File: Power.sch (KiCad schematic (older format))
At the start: 0 parts

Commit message: Power protection and filtering circuit moved to Power.sch, was accidentally on PowerAdjustmentMonitor.sch
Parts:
- added C? (x2): C, symbol C
- added F? (x4): FUSE, symbol FUSE
- added L? (x2): INDUCTOR, symbol INDUCTOR
- added P?: CONN_12X2, symbol CONN_12X2
- added R?: R, symbol R
- added SW?: SWITCH_INV, symbol SWITCH_INV
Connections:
- net labels added: +12P, +12V, +3.3V, +5V, -12P, -12V, GND
- wire segments 0 -> 39

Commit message: Current/fan driver circuit reworked
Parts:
- removed F? (x4): FUSE, symbol FUSE
- added TH? (x4): THERMISTOR, symbol THERMISTOR
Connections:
- net labels added: +12C
- wire segments 39 -> 40
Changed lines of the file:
@@
 $Descr A4 11693 8268
 encoding utf-8
-Sheet 5 9
+Sheet 4 9
 Title ""
 Date ""
@@
 	900  1900 900  2100
 $Comp
-L FUSE F?
-U 1 1 52F29C98
-P 3250 1800
-F 0 "F?" H 3350 1850 40  0000 C CNN
-F 1 "FUSE" H 3150 1750 40  0000 C CNN
-F 2 "" H 3250 1800 60  0000 C CNN
-F 3 "" H 3250 1800 60  0000 C CNN
-	1    3250 1800
-	1    0    0    -1
-$EndComp
-$Comp
-L FUSE F?
-U 1 1 52F29C9E
-P 3750 2000
-F 0 "F?" H 3850 2050 40  0000 C CNN
-F 1 "FUSE" H 3650 1950 40  0000 C CNN
-F 2 "" H 3750 2000 60  0000 C CNN
-F 3 "" H 3750 2000 60  0000 C CNN
-	1    3750 2000
-	1    0    0    -1
-$EndComp
-$Comp
-L FUSE F?
-U 1 1 52F29CA4
-P 4250 2200
-F 0 "F?" H 4350 2250 40  0000 C CNN
-F 1 "FUSE" H 4150 2150 40  0000 C CNN
-F 2 "" H 4250 2200 60  0000 C CNN
-F 3 "" H 4250 2200 60  0000 C CNN
-	1    4250 2200
-	1    0    0    -1
-$EndComp
-$Comp
-L FUSE F?
-U 1 1 52F29CAA
-P 4750 2400
-F 0 "F?" H 4850 2450 40  0000 C CNN
-F 1 "FUSE" H 4650 2350 40  0000 C CNN
-F 2 "" H 4750 2400 60  0000 C CNN
-F 3 "" H 4750 2400 60  0000 C CNN
-	1    4750 2400
-	1    0    0    -1
-$EndComp
-$Comp
 L SWITCH_INV SW?
 U 1 1 52F29CB0
@@
 	-1   0    0    1
 $EndComp
+Connection ~ 2800 2200
+Wire Wire Line
+	2800 2200 2800 1550
+$Comp
+L +12C #PWR?
+U 1 1 52FBE7EF
+P 2800 1550
+F 0 "#PWR?" H 2800 1520 30  0001 C CNN
+F 1 "+12C" H 2800 1660 40  0000 C CNN
+F 2 "" H 2800 1550 60  0000 C CNN
+F 3 "" H 2800 1550 60  0000 C CNN
+	1    2800 1550
+	1    0    0    -1
+$EndComp
+$Comp
+L THERMISTOR TH?
+U 1 1 52FBEC4C
+P 3250 1800
+F 0 "TH?" V 3350 1850 50  0000 C CNN
+F 1 "THERMISTOR" V 3150 1800 50  0000 C CNN
+F 2 "" H 3250 1800 60  0000 C CNN
+F 3 "" H 3250 1800 60  0000 C CNN
+	1    3250 1800
+	0    -1   -1   0
+$EndComp
+$Comp
+L THERMISTOR TH?
+U 1 1 52FBEC68
+P 3750 2000
+F 0 "TH?" V 3850 2050 50  0000 C CNN
+F 1 "THERMISTOR" V 3650 2000 50  0000 C CNN
+F 2 "" H 3750 2000 60  0000 C CNN
+F 3 "" H 3750 2000 60  0000 C CNN
+	1    3750 2000
+	0    -1   -1   0
+$EndComp
+$Comp
+L THERMISTOR TH?
+U 1 1 52FBEC73
+P 4250 2200
+F 0 "TH?" V 4350 2250 50  0000 C CNN
+F 1 "THERMISTOR" V 4150 2200 50  0000 C CNN
+F 2 "" H 4250 2200 60  0000 C CNN
+F 3 "" H 4250 2200 60  0000 C CNN
+	1    4250 2200
+	0    -1   -1   0
+$EndComp
+$Comp
+L THERMISTOR TH?
+U 1 1 52FBEC7E
+P 4750 2400
+F 0 "TH?" V 4850 2450 50  0000 C CNN
+F 1 "THERMISTOR" V 4650 2400 50  0000 C CNN
+F 2 "" H 4750 2400 60  0000 C CNN
+F 3 "" H 4750 2400 60  0000 C CNN
+	1    4750 2400
+	0    -1   -1   0
+$EndComp
 $EndSCHEMATC

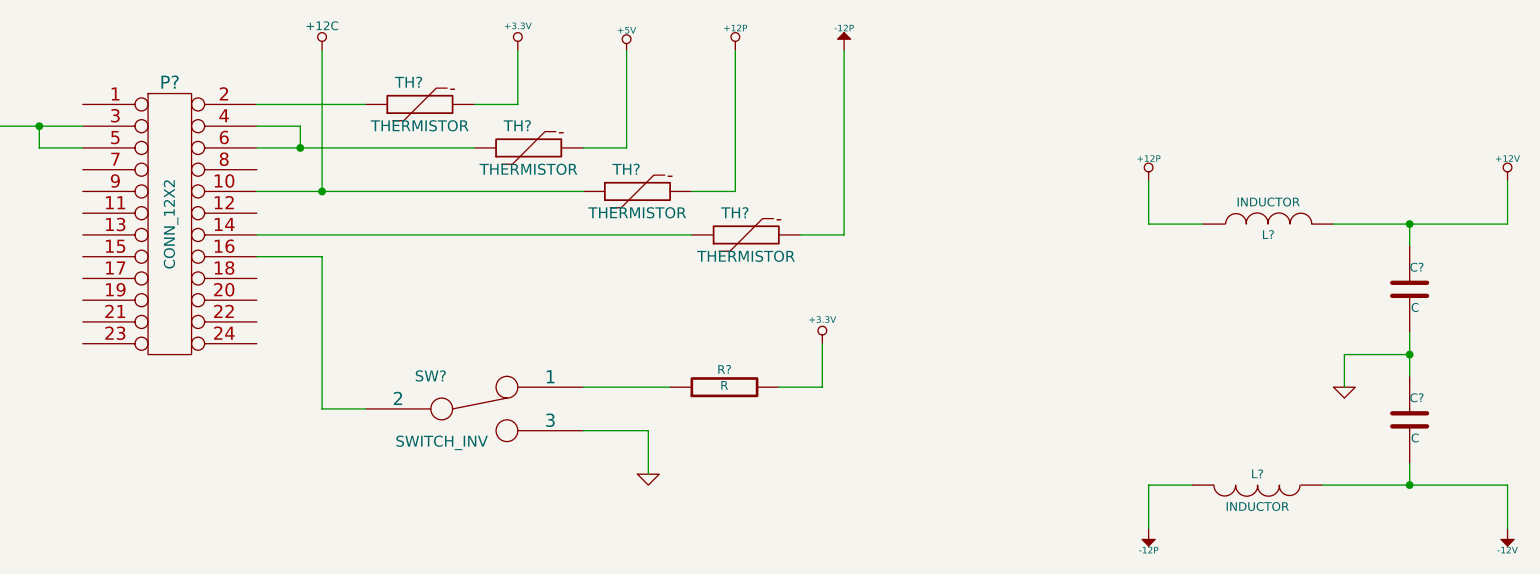
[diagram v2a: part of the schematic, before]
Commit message: Added footprints for the relay module, preliminarily annotated schematic, relay components placed on PCB
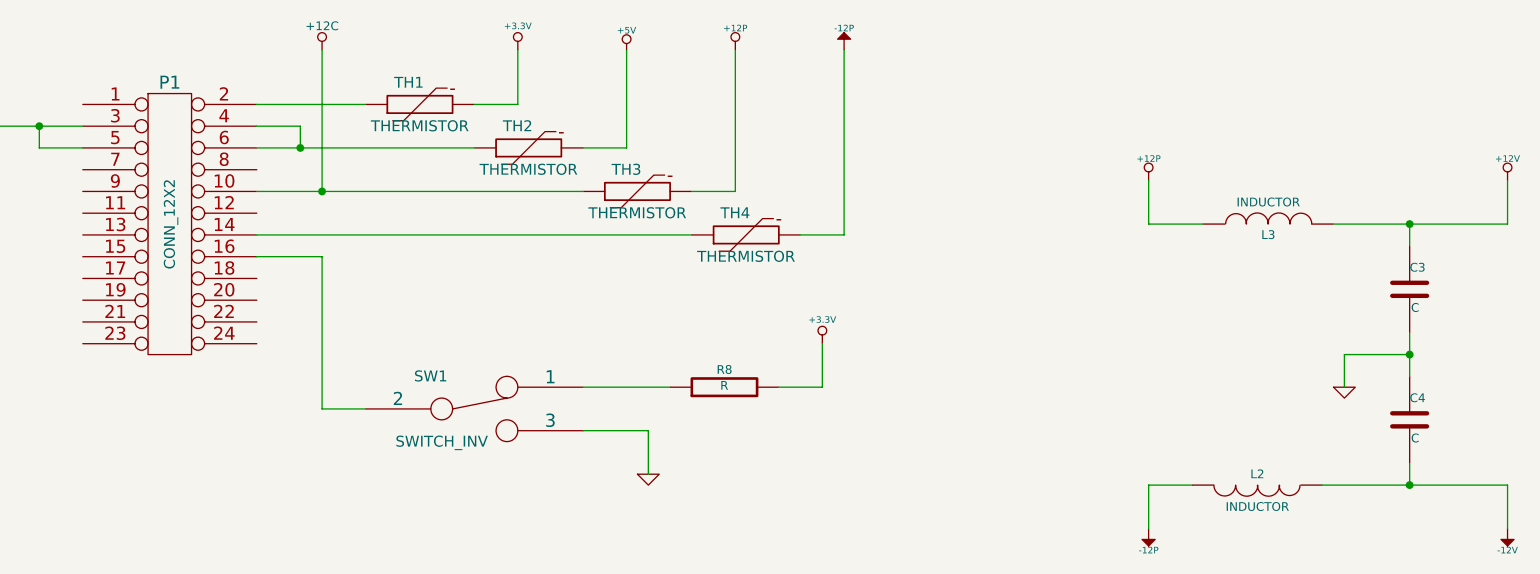
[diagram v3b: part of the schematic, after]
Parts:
- gave numbers to parts that had none: 11
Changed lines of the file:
@@
 $EndDescr
 $Comp
-L CONN_12X2 P?
+L CONN_12X2 P1
 U 1 1 52F29C7F
 P 2100 2350
-F 0 "P?" H 2100 3000 60  0000 C CNN
+F 0 "P1" H 2100 3000 60  0000 C CNN
 F 1 "CONN_12X2" V 2100 2350 50  0000 C CNN
 F 2 "" H 2100 2350 60  0000 C CNN
@@
 $EndComp
 $Comp
-L GND #PWR?
+L GND #PWR7
 U 1 1 52F29C85
 P 900 2100
-F 0 "#PWR?" H 900 2100 30  0001 C CNN
+F 0 "#PWR7" H 900 2100 30  0001 C CNN
 F 1 "GND" H 900 2030 30  0001 C CNN
 F 2 "" H 900 2100 60  0000 C CNN
@@
 $EndComp
 $Comp
-L +3.3V #PWR?
+L +3.3V #PWR9
 U 1 1 52F29C8B
 P 3700 1550
-F 0 "#PWR?" H 3700 1510 30  0001 C CNN
+F 0 "#PWR9" H 3700 1510 30  0001 C CNN
 F 1 "+3.3V" H 3700 1660 30  0000 C CNN
 F 2 "" H 3700 1550 60  0000 C CNN
@@
 $EndComp
 $Comp
-L +5V #PWR?
+L +5V #PWR10
 U 1 1 52F29C91
 P 4200 1550
-F 0 "#PWR?" H 4200 1640 20  0001 C CNN
+F 0 "#PWR10" H 4200 1640 20  0001 C CNN
 F 1 "+5V" H 4200 1640 30  0000 C CNN
 F 2 "" H 4200 1550 60  0000 C CNN
@@
 	900  1900 900  2100
 $Comp
-L SWITCH_INV SW?
+L SWITCH_INV SW1
 U 1 1 52F29CB0
 P 3500 3200
-F 0 "SW?" H 3300 3350 50  0000 C CNN
+F 0 "SW1" H 3300 3350 50  0000 C CNN
 F 1 "SWITCH_INV" H 3350 3050 50  0000 C CNN
 F 2 "" H 3500 3200 60  0000 C CNN
@@
 	4700 2200 4700 1550
 $Comp
-L +12P #PWR?
+L +12P #PWR12
 U 1 1 52F29CC3
 P 4700 1550
-F 0 "#PWR?" H 4700 1520 30  0001 C CNN
+F 0 "#PWR12" H 4700 1520 30  0001 C CNN
 F 1 "+12P" H 4700 1650 30  0000 C CNN
 F 2 "" H 4700 1550 60  0000 C CNN
@@
 	5200 2400 5200 1550
 $Comp
-L -12P #PWR?
+L -12P #PWR14
 U 1 1 52F29CCB
 P 5200 1550
-F 0 "#PWR?" H 5200 1680 20  0001 C CNN
+F 0 "#PWR14" H 5200 1680 20  0001 C CNN
 F 1 "-12P" H 5200 1650 30  0000 C CNN
 F 2 "" H 5200 1550 60  0000 C CNN
@@
 	4300 3300 4300 3500
 $Comp
-L GND #PWR?
+L GND #PWR11
 U 1 1 52F29CDA
 P 4300 3500
-F 0 "#PWR?" H 4300 3500 30  0001 C CNN
+F 0 "#PWR11" H 4300 3500 30  0001 C CNN
 F 1 "GND" H 4300 3430 30  0001 C CNN
 F 2 "" H 4300 3500 60  0000 C CNN
@@
 $EndComp
 $Comp
-L R R?
+L R R8
 U 1 1 52F29CE0
 P 4650 3100
-F 0 "R?" V 4730 3100 40  0000 C CNN
+F 0 "R8" V 4730 3100 40  0000 C CNN
 F 1 "R" V 4657 3101 40  0000 C CNN
 F 2 "" V 4580 3100 30  0000 C CNN
@@
 	5100 3100 5100 2900
 $Comp
-L +3.3V #PWR?
+L +3.3V #PWR13
 U 1 1 52F29CE9
 P 5100 2900
-F 0 "#PWR?" H 5100 2860 30  0001 C CNN
+F 0 "#PWR13" H 5100 2860 30  0001 C CNN
 F 1 "+3.3V" H 5100 3010 30  0000 C CNN
 F 2 "" H 5100 2900 60  0000 C CNN
@@
 $EndComp
 $Comp
-L +12P #PWR?
+L +12P #PWR15
 U 1 1 52F29CEF
 P 6600 2150
-F 0 "#PWR?" H 6600 2120 30  0001 C CNN
+F 0 "#PWR15" H 6600 2120 30  0001 C CNN
 F 1 "+12P" H 6600 2250 30  0000 C CNN
 F 2 "" H 6600 2150 60  0000 C CNN
@@
 $EndComp
 $Comp
-L -12P #PWR?
+L -12P #PWR16
 U 1 1 52F29CF5
 P 6600 3750
-F 0 "#PWR?" H 6600 3880 20  0001 C CNN
+F 0 "#PWR16" H 6600 3880 20  0001 C CNN
 F 1 "-12P" H 6600 3850 30  0000 C CNN
 F 2 "" H 6600 3750 60  0000 C CNN
@@
 $EndComp
 $Comp
-L GND #PWR?
+L GND #PWR17
 U 1 1 52F29CFB
 P 7500 3100
-F 0 "#PWR?" H 7500 3100 30  0001 C CNN
+F 0 "#PWR17" H 7500 3100 30  0001 C CNN
 F 1 "GND" H 7500 3030 30  0001 C CNN
 F 2 "" H 7500 3100 60  0000 C CNN
@@
 $EndComp
 $Comp
-L INDUCTOR L?
+L INDUCTOR L3
 U 1 1 52F29D01
 P 7150 2350
-F 0 "L?" V 7100 2350 40  0000 C CNN
+F 0 "L3" V 7100 2350 40  0000 C CNN
 F 1 "INDUCTOR" V 7250 2350 40  0000 C CNN
 F 2 "" H 7150 2350 60  0000 C CNN
@@
 $EndComp
 $Comp
-L INDUCTOR L?
+L INDUCTOR L2
 U 1 1 52F29D07
 P 7100 3550
-F 0 "L?" V 7050 3550 40  0000 C CNN
+F 0 "L2" V 7050 3550 40  0000 C CNN
 F 1 "INDUCTOR" V 7200 3550 40  0000 C CNN
 F 2 "" H 7100 3550 60  0000 C CNN
@@
 $EndComp
 $Comp
-L C C?
+L C C4
 U 1 1 52F29D0D
 P 7800 3250
-F 0 "C?" H 7800 3350 40  0000 L CNN
+F 0 "C4" H 7800 3350 40  0000 L CNN
 F 1 "C" H 7806 3165 40  0000 L CNN
 F 2 "" H 7838 3100 30  0000 C CNN
@@
 $EndComp
 $Comp
-L C C?
+L C C3
 U 1 1 52F29D13
 P 7800 2650
-F 0 "C?" H 7800 2750 40  0000 L CNN
+F 0 "C3" H 7800 2750 40  0000 L CNN
 F 1 "C" H 7806 2565 40  0000 L CNN
 F 2 "" H 7838 2500 30  0000 C CNN
@@
 Connection ~ 7800 3550
 $Comp
-L +12V #PWR?
+L +12V #PWR18
 U 1 1 52F29D29
 P 8250 2150
-F 0 "#PWR?" H 8250 2100 20  0001 C CNN
+F 0 "#PWR18" H 8250 2100 20  0001 C CNN
 F 1 "+12V" H 8250 2250 30  0000 C CNN
 F 2 "" H 8250 2150 60  0000 C CNN
@@
 $EndComp
 $Comp
-L -12V #PWR?
+L -12V #PWR19
 U 1 1 52F29D2F
 P 8250 3750
-F 0 "#PWR?" H 8250 3880 20  0001 C CNN
+F 0 "#PWR19" H 8250 3880 20  0001 C CNN
 F 1 "-12V" H 8250 3850 30  0000 C CNN
 F 2 "" H 8250 3750 60  0000 C CNN
@@
 	2800 2200 2800 1550
 $Comp
-L +12C #PWR?
+L +12C #PWR8
 U 1 1 52FBE7EF
 P 2800 1550
-F 0 "#PWR?" H 2800 1520 30  0001 C CNN
+F 0 "#PWR8" H 2800 1520 30  0001 C CNN
 F 1 "+12C" H 2800 1660 40  0000 C CNN
 F 2 "" H 2800 1550 60  0000 C CNN
@@
 $EndComp
 $Comp
-L THERMISTOR TH?
+L THERMISTOR TH1
 U 1 1 52FBEC4C
 P 3250 1800
-F 0 "TH?" V 3350 1850 50  0000 C CNN
+F 0 "TH1" V 3350 1850 50  0000 C CNN
 F 1 "THERMISTOR" V 3150 1800 50  0000 C CNN
 F 2 "" H 3250 1800 60  0000 C CNN
@@
 $EndComp
 $Comp
-L THERMISTOR TH?
+L THERMISTOR TH2
 U 1 1 52FBEC68
 P 3750 2000
-F 0 "TH?" V 3850 2050 50  0000 C CNN
+F 0 "TH2" V 3850 2050 50  0000 C CNN
 F 1 "THERMISTOR" V 3650 2000 50  0000 C CNN
 F 2 "" H 3750 2000 60  0000 C CNN
@@
 $EndComp
 $Comp
-L THERMISTOR TH?
+L THERMISTOR TH3
 U 1 1 52FBEC73
 P 4250 2200
-F 0 "TH?" V 4350 2250 50  0000 C CNN
+F 0 "TH3" V 4350 2250 50  0000 C CNN
 F 1 "THERMISTOR" V 4150 2200 50  0000 C CNN
 F 2 "" H 4250 2200 60  0000 C CNN
@@
 $EndComp
 $Comp
-L THERMISTOR TH?
+L THERMISTOR TH4
 U 1 1 52FBEC7E
 P 4750 2400
-F 0 "TH?" V 4850 2450 50  0000 C CNN
+F 0 "TH4" V 4850 2450 50  0000 C CNN
 F 1 "THERMISTOR" V 4650 2400 50  0000 C CNN
 F 2 "" H 4750 2400 60  0000 C CNN

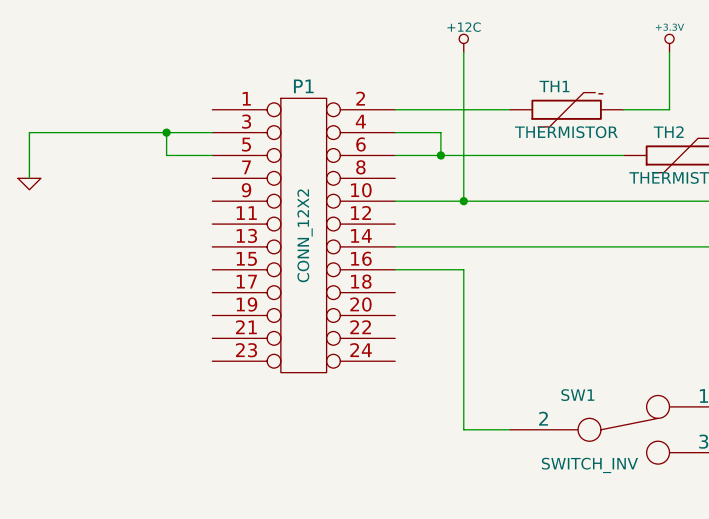
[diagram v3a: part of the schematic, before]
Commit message: Associated and placed the terminal blocks and ATX header
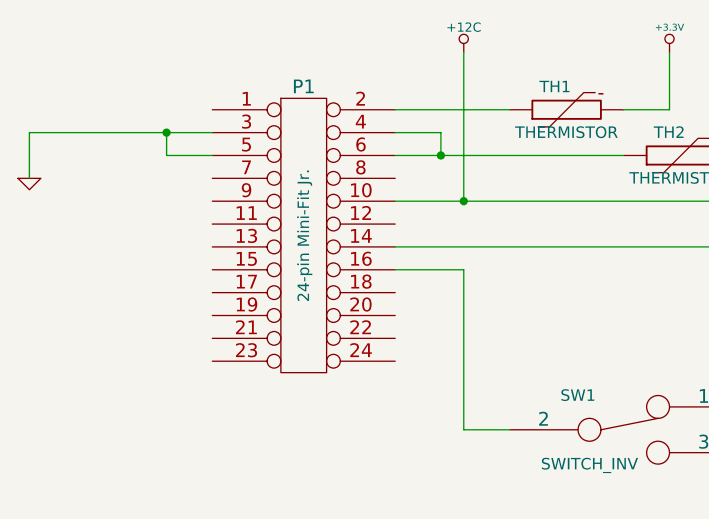
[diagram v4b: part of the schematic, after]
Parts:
- P1: value CONN_12X2 -> 24-pin Mini-Fit Jr.; MFG Name (none) -> Molex; MFG Part Number (none) -> 39-30-1240
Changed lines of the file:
@@
 P 2100 2350
 F 0 "P1" H 2100 3000 60  0000 C CNN
-F 1 "CONN_12X2" V 2100 2350 50  0000 C CNN
+F 1 "24-pin Mini-Fit Jr." V 2100 2350 50  0000 C CNN
 F 2 "" H 2100 2350 60  0000 C CNN
 F 3 "" H 2100 2350 60  0000 C CNN
+F 4 "Molex" H 2100 2350 60  0001 C CNN "MFG Name"
+F 5 "39-30-1240" H 2100 2350 60  0001 C CNN "MFG Part Number"
 	1    2100 2350
 	1    0    0    -1
